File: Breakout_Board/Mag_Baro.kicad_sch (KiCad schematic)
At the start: 8 parts, among them U4 MMC5983MA, U5 BMP581

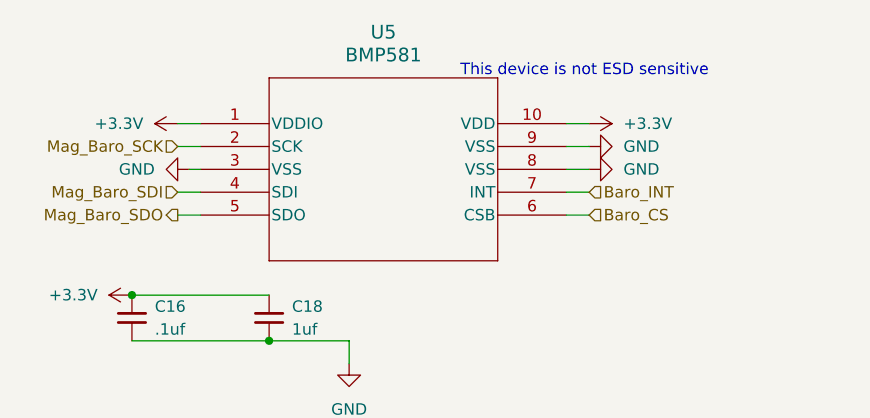
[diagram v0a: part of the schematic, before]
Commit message: Swap BMP581 for BMP585, move ADXL interrupts to PB5/PB6, add J4 GND, clean up library pin types
- Add BMP585 library (symbol + LGA9 footprint) and replace U5
- Move ADXL_INT0/INT1 off PA11/PA12 (USB pins) to PB5/PB6
- J4 now 5-pin with GND
- Set GND/VSS pins to power input in ADXL380, MMC5983MA, BMP585 symbols
- Add library prefix to ADXL380 symbol footprint field

Co-Authored-By: Claude Sonnet 5.5 <noreply@anthropic.com>
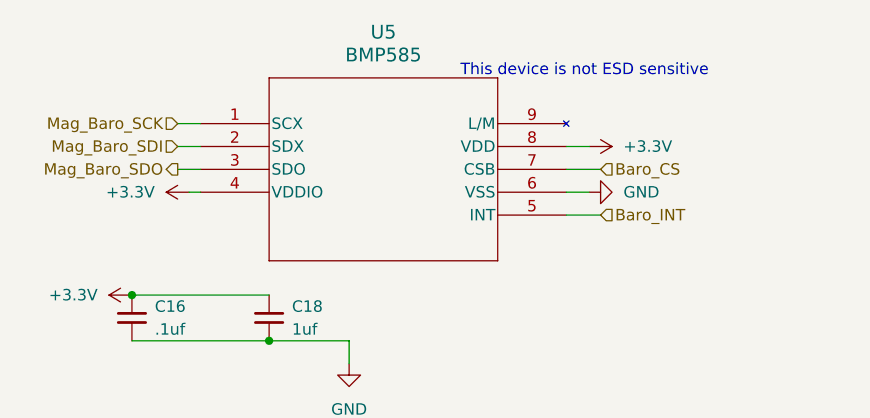
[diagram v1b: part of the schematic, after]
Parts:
- U5: value BMP581 -> BMP585; footprint BMP581:QFN10_BMP581_BOS -> BMP585:LGA9_BMP585_BOS; symbol BMP581:BMP581 -> BMP585:BMP585
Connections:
- net +3.3V: now also U5.4 (VDDIO), U5.8 (VDD); no longer U5.1 (VDDIO), U5.10 (VDD)
- net Baro_CS: now also U5.7 (CSB); no longer U5.6 (CSB)
- net Baro_INT: now also U5.5 (INT); no longer U5.7 (INT)
- net GND: now also U5.6 (VSS); no longer U5.3 (VSS), U5.8 (VSS), U5.9 (VSS)
- net Mag_Baro_SCK: now also U5.1 (SCX); no longer U5.2 (SCK)
- net Mag_Baro_SDI: now also U5.2 (SDX); no longer U5.4 (SDI)
- net Mag_Baro_SDO: now also U5.3 (SDO); no longer U5.5 (SDO)
